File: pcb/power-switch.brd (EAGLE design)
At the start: 100 x 52 mm, 22 parts, among them CON1 KF301-3P, CON2 KF301-3P, K1 SMIH-12VDC-S-L-C, K2 SMIH-12VDC-S-L-C, U1 MCP1631X, U6 EFM32PG1B200_Q32, U7 RFM69HW

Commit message: PCB Work
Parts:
- added C4: 1uF, Capacitor:CAP1206
- added C5: 100nF, Capacitor:CAP0603
- added D1, D2: B0530W, Generic Diode:SOD-123
- added D3: SMAJ12A, TVS:DO214AC
- added F1: 500mA Hold, PTC Fuses:1812
- added Q1, Q2: AO3400, Alpha Omega:SOT23
- added R1, R3: 22 Ohms, Resistor:RES0603
- added R2, R5: 100K Ohms, Resistor:RES0603
- moved TC1 115.7 mm to (91.6, 39.1), turned to 90 degrees
- moved U7 93.3 mm to (72.0, 13.0)
- moved U1 27.2 mm to (-45.2, 30.0)
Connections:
- new net K1_EN: R1.2
- new net K2_EN: R3.2
- new net N$2: Q1.1, R1.1, R2.1
- new net N$3: D1.A, K1.COIL2, Q1.3
- new net N$4: Q2.1, R3.1, R5.1
- new net N$5: D2.A, K2.COIL2, Q2.3
- new net N$7: ACDC1.+VO, F1.2
- net 12V0: now also C4.1, C5.1, D1.C, D2.C, D3.C, F1.1, K1.COIL1, K2.COIL1; no longer ACDC1.+VO
- net GND: now also ACDC1.-VO, C4.2, C5.2, D3.A, Q1.2, Q2.2, R2.2, R5.2
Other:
- outline, holes or cut-outs redrawn

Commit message: PCB Work
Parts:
- removed C4: 1uF, Capacitor:CAP1206
- added C10, C11, C12, C13, C20, C6: 100nF, Capacitor:CAP0603
- added C7: 1uF, Capacitor:CAP0603
- added C8, C9: 100uF, Capacitor:CAP1206
- added CON3: 4P-SH-TOP, JST:SH-04-TOP
- added L2: 15uH, Inductor:IND2520
- added R10, R15, R6, R8, R9: 10K Ohms, Resistor:RES0603
- added R16: 100K Ohms, Resistor:RES0603
- added R7: 31.6K Ohms, Resistor:RES0603
- added U2: MCP9802, Microchip:SOT23-5
- added U8: SST26VF016B, Microchip:WSOIC8
- added X1: 40MHz, Crystal:4-SMD-3225
- R14, R4: value 10K Ohms -> 100K Ohms
- TC1: value TC2050-IDC -> TC2050-IDC-NL; device TagConnect:TC2050-IDC -> TagConnect:TC2050-IDC-NL
- moved C5 138.5 mm to (71.8, 20.5), turned to 270 degrees
- moved D3 130.2 mm to (66.1, 20.5), turned to 270 degrees
- moved F1 124.3 mm to (62.0, 20.5), turned to 270 degrees
- moved R1 122.6 mm to (67.0, 48.0), turned to 90 degrees
- moved R2 121.7 mm to (65.1, 48.0), turned to 90 degrees
- moved R14 121.6 mm to (85.5, 9.50), turned to 90 degrees
- moved S1 121.3 mm to (79.0, 48.0), flipped to the bottom, turned to 180 degrees
- moved R3 120.6 mm to (67.7, 12.8), turned to 90 degrees
- moved R5 118.0 mm to (65.8, 12.8), turned to 90 degrees
- moved Q1 116.5 mm to (62.0, 48.0), turned to 180 degrees
- moved Q2 115.2 mm to (62.5, 12.8), turned to 180 degrees
- moved D1 113.6 mm to (59.0, 43.0), turned to 90 degrees
- moved C19 113.3 mm to (72.7, 35.2), turned to 270 degrees
- moved L1 110.9 mm to (70.1, 36.0), turned to 180 degrees
- moved U1 110.2 mm to (65.0, 28.0), turned to 270 degrees
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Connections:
- new net !FLASH_CS: R16.1, U8.1
- new net BTN1: C13.1, CON3.2, R10.1
- new net BTN2: C12.1, CON3.3, R9.1
- new net I2C0_SCL: R15.1, U2.4
- new net I2C0_SDA: R8.1, U2.5
- new net N$10: R6.2, R7.1, U1.1
- new net N$16: U6.6, X1.1
- new net N$17: U6.7, X1.3
- new net N$6: C6.2, L2.1, U1.6
- new net N$8: C6.1, U1.7
- new net N$9: C7.1, U1.2
- new net TEMP_ALERT: U2.3
- net 12V0: now also C8.1, U1.3, U1.4; no longer C4.1
- net 3V3: now also C10.1, C11.1, C20.1, C9.1, L2.2, R10.2, R15.2, R16.2, R7.2, R8.2, R9.2, U2.1, U8.3, U8.7, U8.8
- net GND: now also C10.2, C11.2, C12.2, C13.2, C20.2, C7.2, C8.2, C9.2, CON3.1, CON3.4, R6.1, U1.5, U1.8, U2.2, U8.4, X1.2, X1.4; no longer C4.2
- net US0_CLK: now also U8.6
- net US0_MISO: now also U8.2
- net US0_MOSI: now also U8.5
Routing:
- net 12V0: track 0.00 -> 79.7 mm
- net 3V3: track 0.00 -> 41.3 mm
- net N$5: track 0.00 -> 9.49 mm
- net N$3: track 0.00 -> 9.49 mm
- net N$7: track 0.00 -> 7.60 mm
- net N$10: track 0.00 -> 6.84 mm
- net N$20: track 0.00 -> 6.24 mm
- net N$6: track 0.00 -> 5.66 mm
- net 1V8: track 0.00 -> 5.42 mm
- net N$17: track 0.00 -> 5.33 mm
- net BTN2: track 0.00 -> 5.32 mm
- net BTN1: track 0.00 -> 5.32 mm
- net N$1: track 0.00 -> 4.62 mm, vias 0 -> 1
- net N$4: track 0.00 -> 4.18 mm
- net N$2: track 0.00 -> 3.98 mm
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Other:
- board size 100 x 52 mm -> 91 x 52 mm

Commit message: Finished PCB
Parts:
- added D4, D5: LED1206, LED:1206
- added LOGO1: HV_WARNING, Silkscreen:HV_WARNING
- added R11, R12: 2.2K Ohms, Resistor:RES0603
- moved C2 11.9 mm to (80.0, 46.5), turned to 90 degrees
- moved C3 1.84 mm to (64.6, 42.1), turned to 90 degrees
- moved D2 1.00 mm to (59.0, 9.00)
- moved C11 0.81 mm to (69.7, 13.6)
- moved R5 0.81 mm to (65.9, 13.6)
- moved Q2 0.81 mm to (62.6, 13.6)
- moved R3 0.81 mm to (67.8, 13.6)
- moved C18 0.20 mm to (74.3, 35.2)
- moved C19 0.20 mm to (72.5, 35.2)
- moved L1 0.20 mm to (69.9, 36.0)
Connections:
- removed net TEMP_ALERT: U2.3
- new net N$11: D4.2, R11.1
- new net N$12: D5.2, R12.1
- net !FLASH_CS: now also U6.32
- net !RFM_CS: now also U6.20; no longer U6.13
- net 12V0: now also R11.2, R12.2
- net BTN1: now also U6.10
- net BTN2: now also U6.11
- net I2C0_SCL: now also U6.14
- net I2C0_SDA: now also U6.13
- net K1_EN: now also U6.17
- net K2_EN: now also U6.18
- net N$3: now also D4.1
- net N$5: now also D5.1
- net RFM_RST: now also U6.19; no longer U6.12
- net US0_CLK: now also U6.21; no longer U6.14
- net US0_MISO: now also U6.24; no longer U6.16
- net US0_MOSI: now also U6.23; no longer U6.15
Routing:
- net 3V3: track 41.3 -> 140.1 mm, vias 0 -> 12
- net !RFM_CS: track 0.00 -> 64.6 mm, vias 0 -> 2
- net RFM_IRQ: track 0.00 -> 60.9 mm, vias 0 -> 3
- net !FLASH_CS: track 0.00 -> 60.9 mm, vias 0 -> 4
- net RFM_RST: track 0.00 -> 59.8 mm, vias 0 -> 2
- net US0_MISO: track 0.00 -> 52.1 mm, vias 0 -> 4
- net K2_EN: track 0.00 -> 48.1 mm, vias 0 -> 2
- net US0_CLK: track 0.00 -> 46.2 mm, vias 0 -> 2
- net US0_MOSI: track 0.00 -> 44.5 mm, vias 0 -> 3
- net BTN1: track 5.32 -> 44.7 mm, vias 0 -> 2
- net BTN2: track 5.32 -> 39.4 mm, vias 0 -> 2
- net I2C0_SCL: track 0.00 -> 31.2 mm, vias 0 -> 2
- net I2C0_SDA: track 0.00 -> 28.9 mm, vias 0 -> 2
- net !RST: track 0.00 -> 18.8 mm, vias 0 -> 2
- net SWO: track 0.00 -> 11.4 mm, vias 0 -> 2
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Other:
- outline, holes or cut-outs redrawn
- board text added: "L OUT1 L IN L OUT2"
- board text added: "N"

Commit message: Update libs
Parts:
- U1: value MCP1631X -> MCP16311
- U2: value MCP9802 -> MCP9802-A0
- U6: value EFM32PG1B200_Q32 -> EFM32PG1B200F256GM32
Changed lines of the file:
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@@
 <drawing>
 <settings>
-<setting alwaysvectorfont="yes"/>
+<setting alwaysvectorfont="no"/>
 <setting verticaltext="up"/>
 </settings>
@@
 <attribute name="VALUE" x="77.325" y="42.945" size="0.762" layer="27" font="vector" ratio="10" rot="R270"/>
 </element>
-<element name="U6" library="EFM32" package="QFN32" value="EFM32PG1B200_Q32" x="71" y="42" smashed="yes" rot="R180">
+<element name="U6" library="EFM32" package="QFN32" value="EFM32PG1B200F256GM32" x="71" y="42" smashed="yes" rot="R180">
 <attribute name="NAME" x="68" y="45.6" size="0.762" layer="25" font="vector" ratio="10" rot="R180"/>
 </element>
@@
 <attribute name="NAME" x="61.272" y="20.262" size="0.762" layer="26" font="vector" ratio="10" rot="MR180"/>
 </element>
-<element name="U1" library="Microchip" package="MSOP8" value="MCP1631X" x="65" y="28" smashed="yes" rot="R270">
+<element name="U1" library="Microchip" package="MSOP8" value="MCP16311" x="65" y="28" smashed="yes" rot="R270">
 <attribute name="NAME" x="64.416" y="25.3825" size="0.762" layer="25" font="vector" ratio="10"/>
 <attribute name="VALUE" x="62.516" y="24.911" size="0.762" layer="27" font="vector" ratio="10"/>
@@
 <attribute name="VALUE" x="82.0536" y="29.968" size="0.762" layer="27" font="vector" ratio="10" rot="SR0"/>
 </element>
-<element name="U2" library="Microchip" package="SOT23-5" value="MCP9802" x="87" y="36" smashed="yes" rot="R90">
+<element name="U2" library="Microchip" package="SOT23-5" value="MCP9802-A0" x="87" y="36" smashed="yes" rot="R90">
 <attribute name="NAME" x="85.1175" y="35.386" size="0.762" layer="25" font="vector" ratio="10" rot="R90"/>
 <attribute name="VALUE" x="90.089" y="34.786" size="0.762" layer="27" font="vector" ratio="10" rot="R90"/>

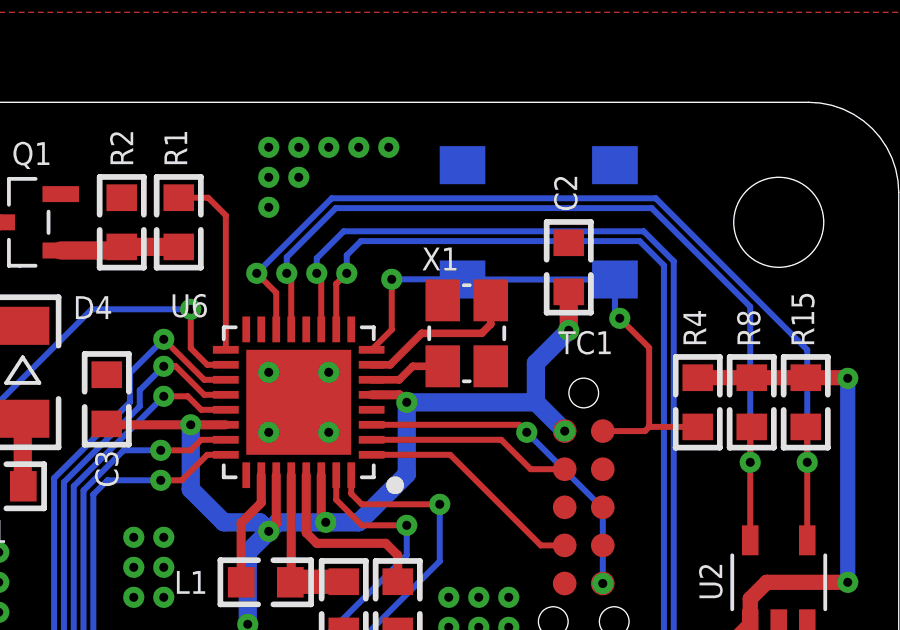
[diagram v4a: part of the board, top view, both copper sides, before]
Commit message: Fix crystal package
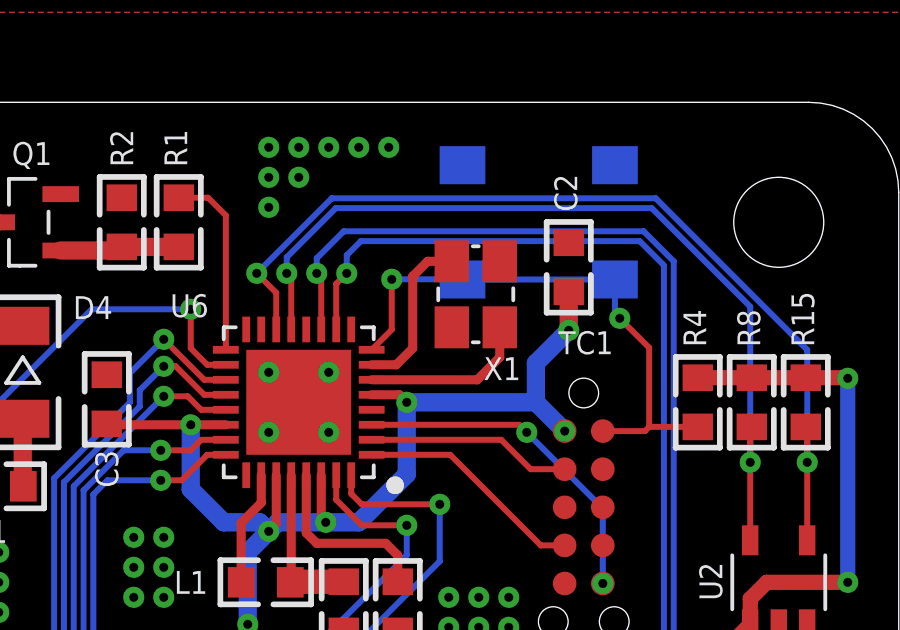
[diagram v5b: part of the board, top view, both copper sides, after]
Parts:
- U6: device EFM32:QFN32 -> EFM32:QFN32_0.5P
- U7: device HopeRF:RFM69W-XXXS2 -> HopeRF:RFM69XW-XXXS2
- moved X1 1.33 mm to (76.9, 45.6), turned to 270 degrees
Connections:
- net GND: now also X1.1, X1.3; no longer X1.2, X1.4
- net N$16: now also X1.2; no longer X1.1
- net N$17: now also X1.4; no longer X1.3
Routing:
- net N$16: track 2.56 -> 5.58 mm
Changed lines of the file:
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@@
 <?xml version="1.0" encoding="utf-8"?>
 <!DOCTYPE eagle SYSTEM "eagle.dtd">
-<eagle version="9.3.2">
+<eagle version="9.4.2">
 <drawing>
 <settings>
@@
 <attribute name="VALUE" x="77.325" y="42.945" size="0.762" layer="27" font="vector" ratio="10" rot="R270"/>
 </element>
-<element name="U6" library="EFM32" package="QFN32" value="EFM32PG1B200F256GM32" x="71" y="42" smashed="yes" rot="R180">
+<element name="U6" library="EFM32" package="QFN32_0.5P" value="EFM32PG1B200F256GM32" x="71" y="42" smashed="yes" rot="R180">
 <attribute name="NAME" x="68" y="45.6" size="0.762" layer="25" font="vector" ratio="10" rot="R180"/>
 </element>
-<element name="U7" library="HopeRF" package="RFM69W-XXXS2" value="RFM69HW" x="71" y="11" smashed="yes" rot="MR180">
+<element name="U7" library="HopeRF" package="RFM69XW-XXXS2" value="RFM69HW" x="71" y="11" smashed="yes" rot="MR180">
 <attribute name="NAME" x="61.272" y="20.262" size="0.762" layer="26" font="vector" ratio="10" rot="MR180"/>
 </element>
@@
 <attribute name="VALUE" x="89.932" y="38.5456" size="0.762" layer="27" font="vector" ratio="10" rot="SR90"/>
 </element>
-<element name="X1" library="Crystal" package="4-SMD-3225" value="40MHz" x="76.6" y="44.3" smashed="yes" rot="R90">
-<attribute name="NAME" x="76.34" y="47.16" size="0.762" layer="25" font="vector" ratio="10" rot="R180"/>
+<element name="X1" library="Crystal" package="4-SMD-3225" value="40MHz" x="76.9" y="45.6" smashed="yes" rot="R270">
+<attribute name="NAME" x="77.16" y="42.74" size="0.762" layer="25" font="vector" ratio="10"/>
 </element>
 <element name="C20" library="Capacitor" package="CAP0603" value="100nF" x="85" y="32" smashed="yes">
@@
 <contactref element="U8" pad="4"/>
 <contactref element="C11" pad="2"/>
-<contactref element="X1" pad="2"/>
-<contactref element="X1" pad="4"/>
+<contactref element="X1" pad="1"/>
+<contactref element="X1" pad="3"/>
 <contactref element="C20" pad="2"/>
 <contactref element="U2" pad="2"/>
@@
 </signal>
 <signal name="N$16">
-<contactref element="X1" pad="1"/>
+<contactref element="X1" pad="2"/>
 <contactref element="U6" pad="6"/>
-<wire x1="73.43" y1="42.75" x2="74.35" y2="42.75" width="0.254" layer="1"/>
-<wire x1="74.8" y1="43.2" x2="75.8" y2="43.2" width="0.254" layer="1"/>
-<wire x1="74.35" y1="42.75" x2="74.8" y2="43.2" width="0.254" layer="1"/>
+<wire x1="73.43" y1="42.75" x2="76.95" y2="42.75" width="0.3048" layer="1"/>
+<wire x1="77.7" y1="43.5" x2="77.7" y2="44.5" width="0.3048" layer="1"/>
+<wire x1="76.95" y1="42.75" x2="77.7" y2="43.5" width="0.3048" layer="1"/>
 </signal>
 <signal name="N$17">
-<contactref element="X1" pad="3"/>
+<contactref element="X1" pad="4"/>
 <contactref element="U6" pad="7"/>
-<wire x1="73.43" y1="43.25" x2="74.05" y2="43.25" width="0.254" layer="1"/>
-<wire x1="77.4" y1="44.6" x2="77.4" y2="45.4" width="0.254" layer="1"/>
-<wire x1="74.05" y1="43.25" x2="75.1" y2="44.3" width="0.254" layer="1"/>
-<wire x1="75.1" y1="44.3" x2="77.1" y2="44.3" width="0.254" layer="1"/>
-<wire x1="77.1" y1="44.3" x2="77.4" y2="44.6" width="0.254" layer="1"/>
+<wire x1="73.43" y1="43.25" x2="74.25" y2="43.25" width="0.3048" layer="1"/>
+<wire x1="75.3" y1="46.7" x2="76.1" y2="46.7" width="0.3048" layer="1"/>
+<wire x1="74.25" y1="43.25" x2="74.8" y2="43.8" width="0.3048" layer="1"/>
+<wire x1="74.8" y1="43.8" x2="74.8" y2="46.2" width="0.3048" layer="1"/>
+<wire x1="74.8" y1="46.2" x2="75.3" y2="46.7" width="0.3048" layer="1"/>
 </signal>
 <signal name="BTN1">

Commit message: Sync library updates Add schematic PDF
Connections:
- net N$11: now also D4.A; no longer D4.2
- net N$12: now also D5.A; no longer D5.2
- net N$3: now also D4.C; no longer D4.1
- net N$5: now also D5.C; no longer D5.1
